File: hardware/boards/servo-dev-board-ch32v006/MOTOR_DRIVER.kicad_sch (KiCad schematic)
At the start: 18 parts, among them J3 SERVO, U2 DRV8212PDSGR

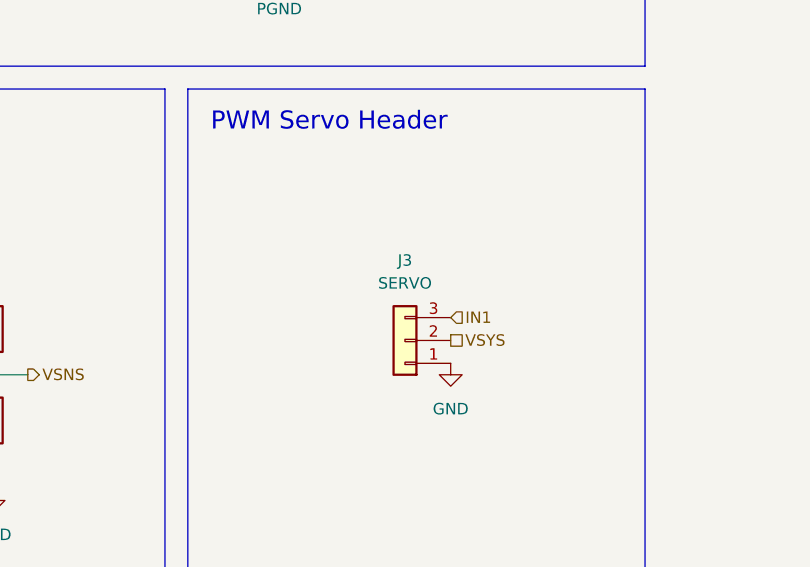
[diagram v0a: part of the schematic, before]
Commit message: update bom and component properties
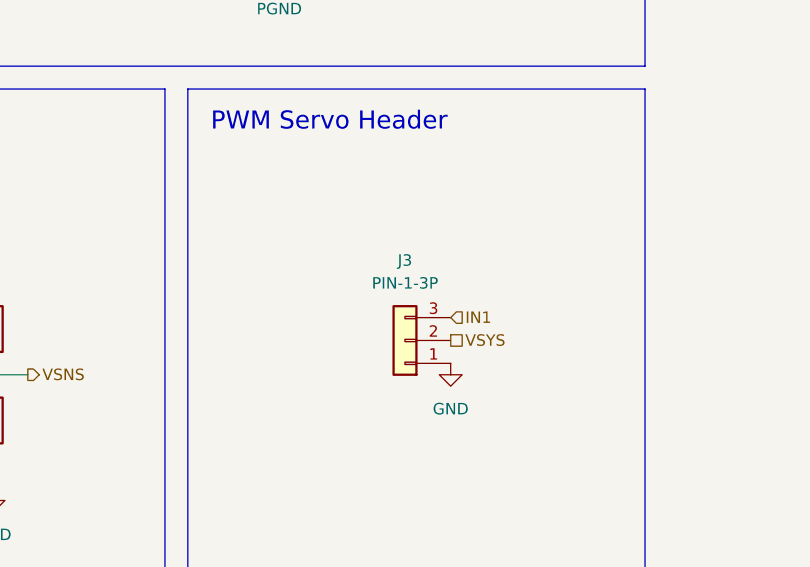
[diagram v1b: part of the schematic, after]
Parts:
- J3: value SERVO -> PIN-1-3P; LCSC (none) -> C49257; MFPN (none) -> 2.54-1*3P
